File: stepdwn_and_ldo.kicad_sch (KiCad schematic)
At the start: 50 parts, among them J1 USB_C_Receptacle_USB2.0_14P, U2 BQ25895RTW, U4 PTPS7A5310AQWRTJQ1, U5 LMS36353QRNLRQ1

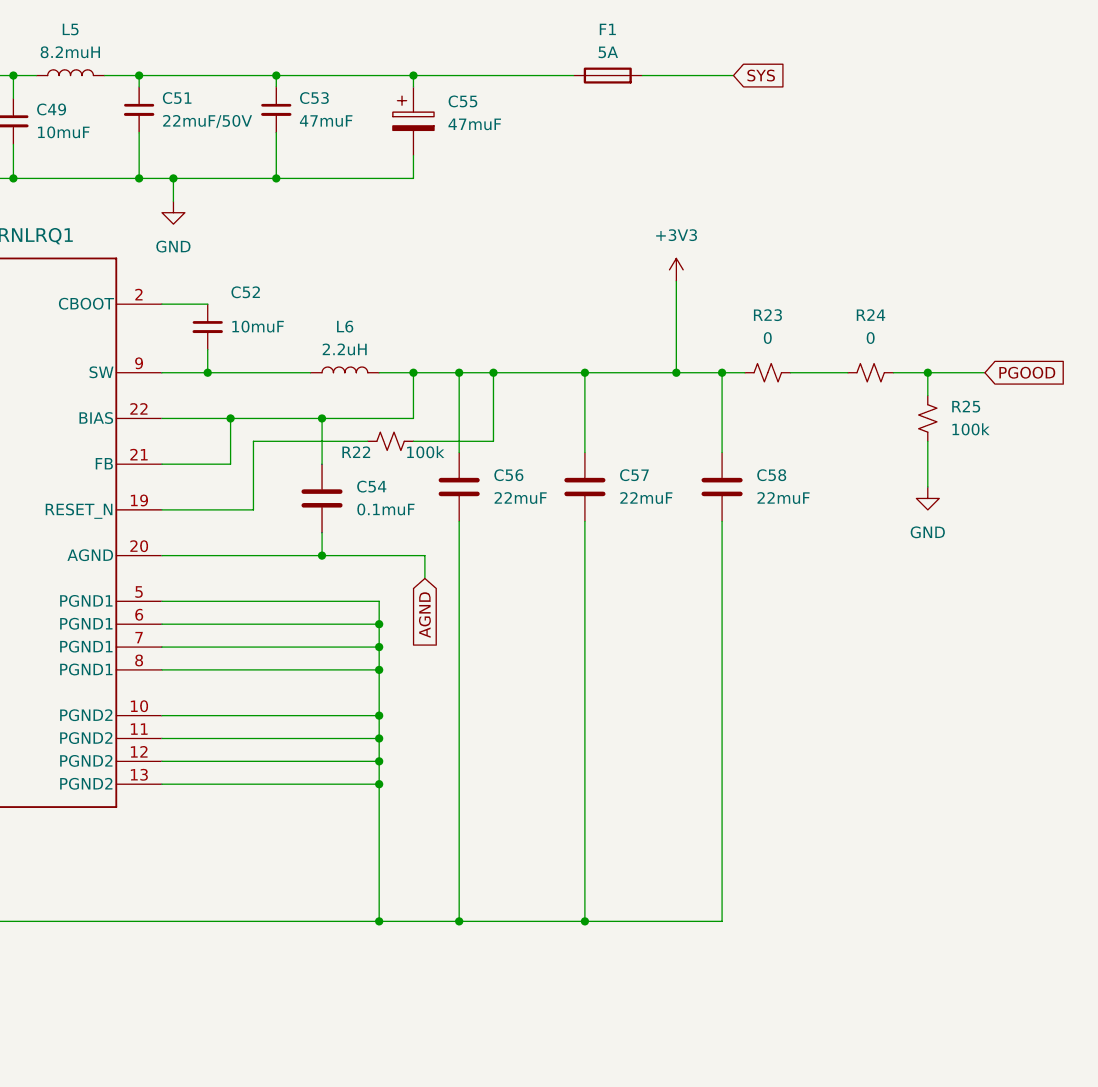
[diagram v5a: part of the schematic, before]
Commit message: editing reset_n pin on LMS3635
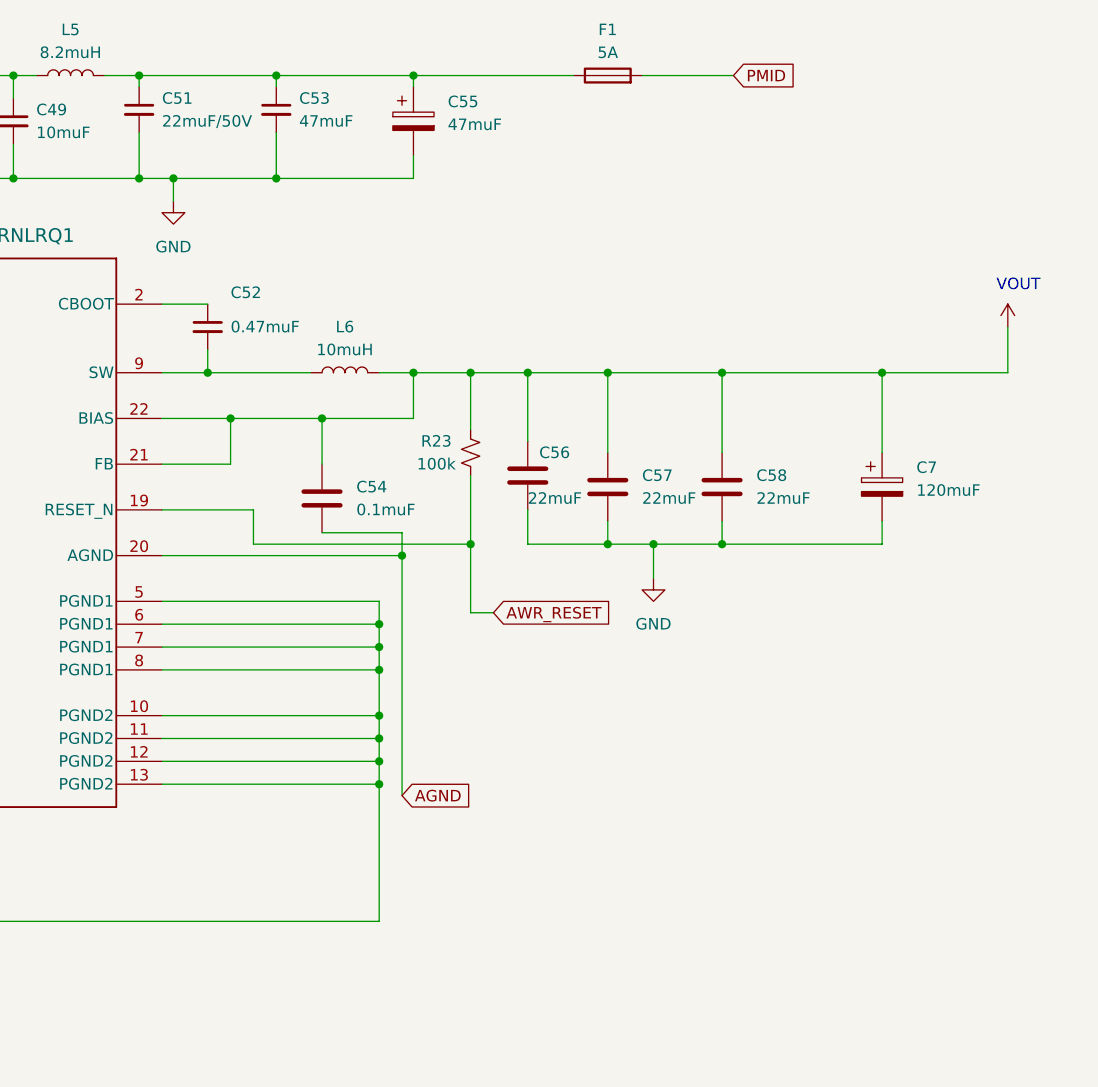
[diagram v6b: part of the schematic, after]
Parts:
- removed R22, R25: 100k, symbol Device:R_Small_US
- removed R24: 0, symbol Device:R_Small_US
- added C7: 120muF, symbol Device:C_Polarized
- C52: value 10muF -> 0.47muF
- L6: value 2.2uH -> 10muH
- R23: value 0 -> 100k
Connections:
- net +3V3: now also R23.2, C7.1; no longer R23.1
- net GND: now also C7.2
- net SYS: no longer F1.2
- net AWR_RESET: now reaches U5.19 (RESET_N)
- net AWR_RESET: now also R23.1
- new net PMID: F1.2
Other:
- note added: "VOUT"
- moved on the sheet: C56, C57

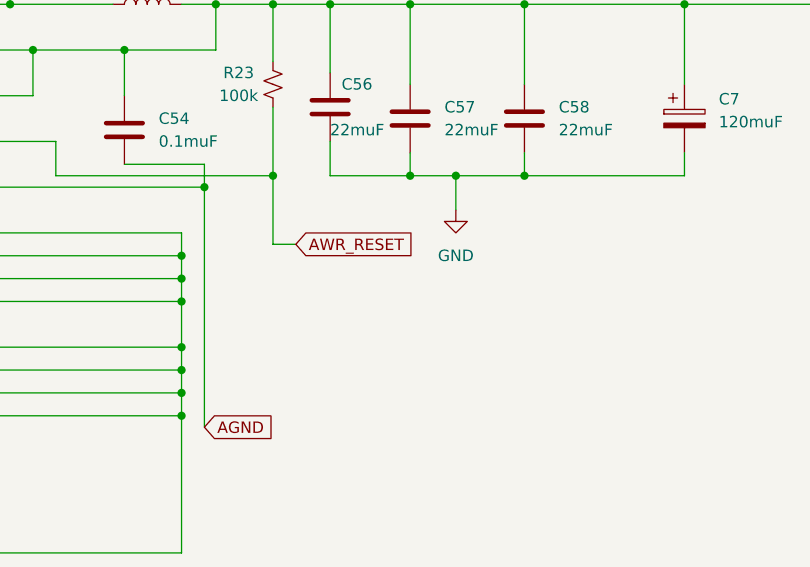
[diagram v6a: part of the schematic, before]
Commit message: making unit design for AWR1843, starting with GND, voltage, I2C and GPIO
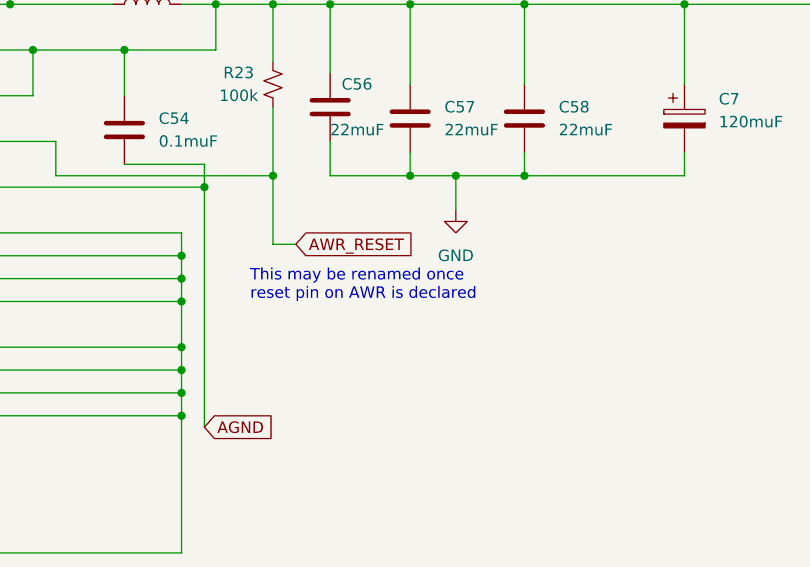
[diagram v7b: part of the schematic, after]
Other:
- note added: "This may be renamed once reset pin on AWR is declared"
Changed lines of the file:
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@@
+    (effects (font (size 1.27 1.27)) (justify left bottom))
+  )
+  (text "This may be renamed once\nreset pin on AWR is declared\n"
+    (at 213.36 86.36 0)
     (effects (font (size 1.27 1.27)) (justify left bottom))
   )

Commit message: working on connectors
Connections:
- net +3V3: now also U4.14 (EN)
- net GND: no longer U4.14 (EN)
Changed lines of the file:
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@@
   (junction (at 138.43 162.56) (diameter 0) (color 0 0 0 0)
+  )
+  (junction (at 93.98 157.48) (diameter 0) (color 0 0 0 0)
   )
   (junction (at 30.48 161.29) (diameter 0) (color 0 0 0 0)
@@
     (stroke (width 0) (type default))
   )
+  (wire (pts (xy 93.98 157.48) (xy 93.98 143.51))
+    (stroke (width 0) (type default))
+  )
   (wire (pts (xy 147.32 162.56) (xy 158.75 162.56))
     (stroke (width 0) (type default))
@@
     (stroke (width 0) (type default))
   )
-  (wire (pts (xy 90.17 165.1) (xy 90.17 170.18))
-    (stroke (width 0) (type default))
-  )
   (wire (pts (xy 205.74 81.28) (xy 205.74 83.82))
     (stroke (width 0) (type default))
@@
     (stroke (width 0) (type default))
   )
-  (wire (pts (xy 93.98 162.56) (xy 93.98 143.51))
+  (wire (pts (xy 93.98 162.56) (xy 93.98 157.48))
     (stroke (width 0) (type default))
   )
@@
     (stroke (width 0) (type default))
   )
+  (wire (pts (xy 90.17 165.1) (xy 90.17 157.48))
+    (stroke (width 0) (type default))
+  )
   (wire (pts (xy 78.74 134.62) (xy 78.74 125.73))
     (stroke (width 0) (type default))
@@
     (stroke (width 0) (type default))
   )
+  (wire (pts (xy 90.17 157.48) (xy 93.98 157.48))
+    (stroke (width 0) (type default))
+  )
